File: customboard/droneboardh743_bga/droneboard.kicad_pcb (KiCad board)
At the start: 4 copper layers, 38 x 38 mm, 67 parts, among them J1 Conn_01x04_MountingPin, J10 Conn_01x03_Pin, J2 Conn_01x04_MountingPin, J3 Conn_01x08_MountingPin, J4 Conn_01x08_MountingPin, J5 USB_C_Receptacle_USB2.0_16P, J6 Conn_01x06_MountingPin, J7 Conn_01x06_MountingPin, Q1 DMN3042L, SW1 434133025816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

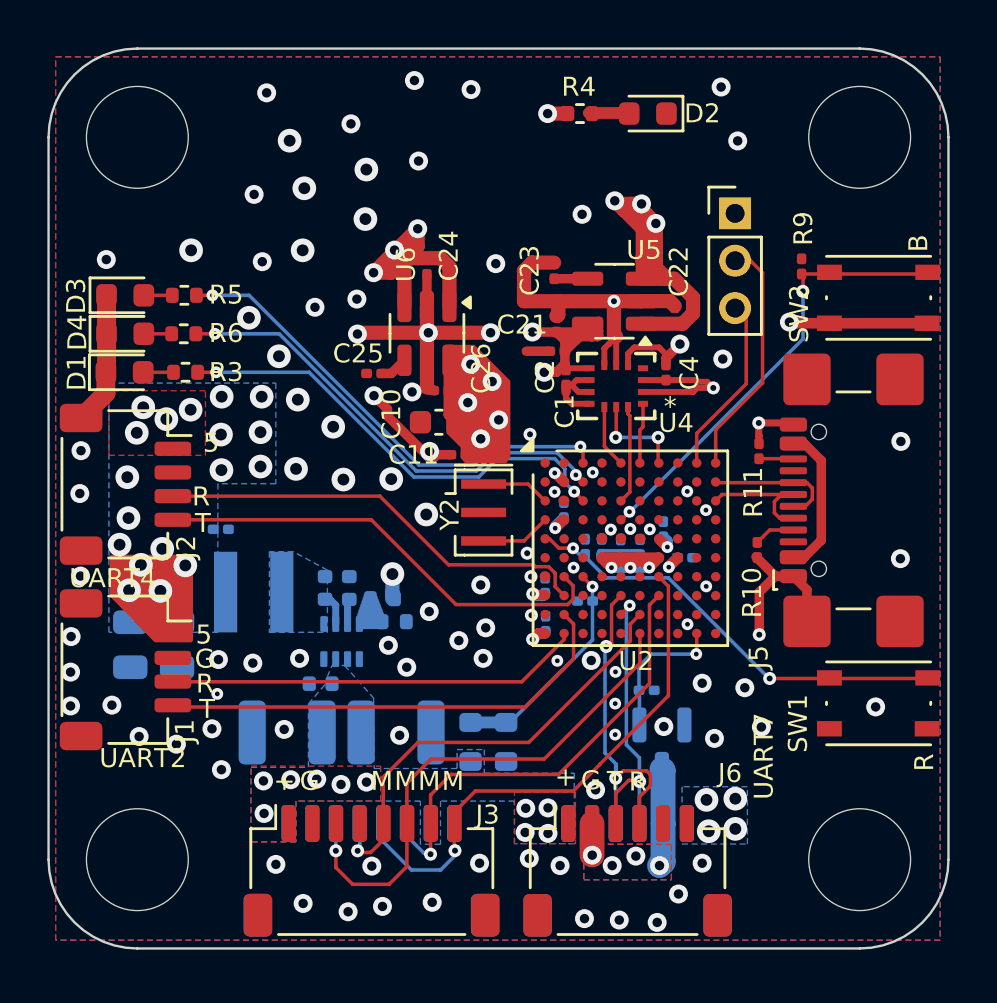
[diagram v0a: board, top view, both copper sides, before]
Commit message: pmos vtx power switching initial
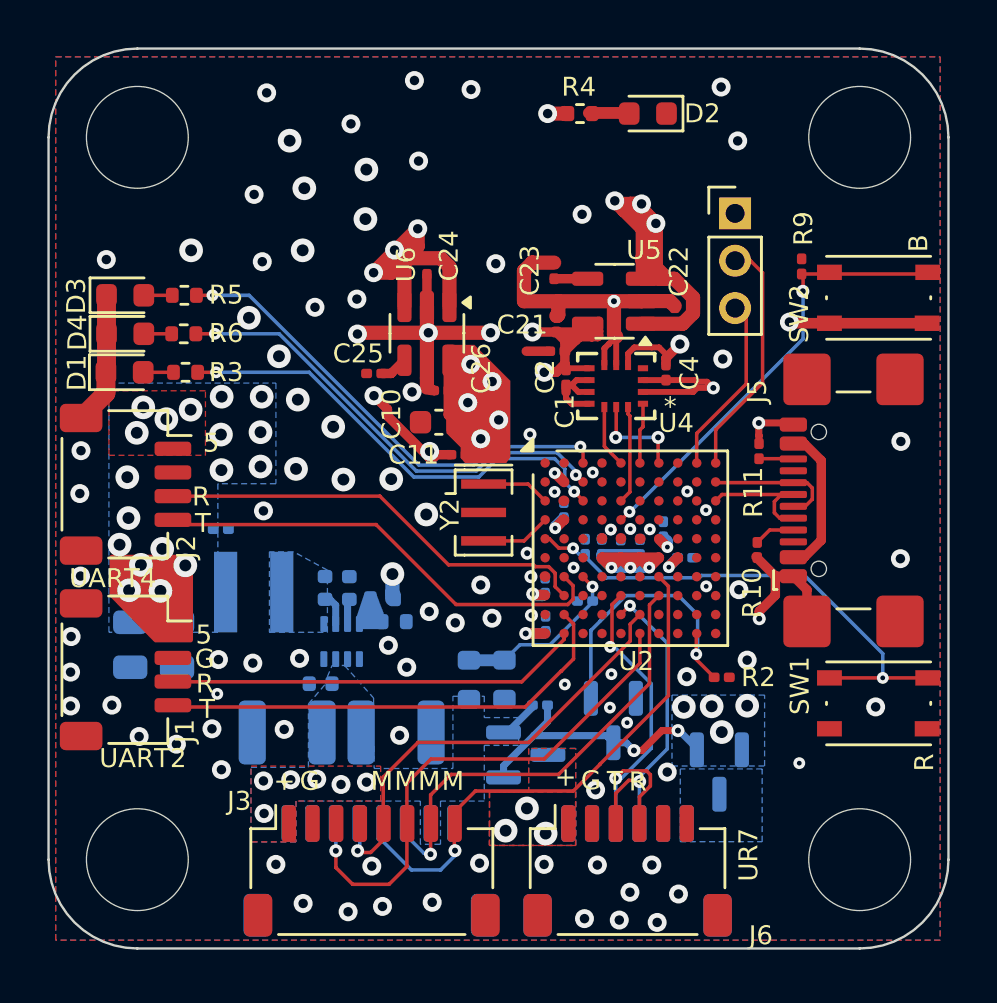
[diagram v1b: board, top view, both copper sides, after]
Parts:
- added Q2: DMP3056L, Package_TO_SOT_SMD:SOT-23, B.Cu at (70.2, 111.8)
- added Q3: DMP3056L, Package_TO_SOT_SMD:SOT-23, B.Cu at (78.3, 112.5)
- added R2: 10K, Resistor_SMD:R_0201_0603Metric, F.Cu at (78.4, 108.5)
- Q1: value DMN3042L -> BSS138-7-F
- moved R1 4.55 mm to (70.8, 109.7)
- moved R8 2.63 mm to (69.2, 108.7)
- moved R7 2.63 mm to (67.8, 108.7)
- moved Q1 2.34 mm to (73.8, 110.4)
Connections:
- J6 pad 1: /12V -> /VTX_12V
- J6 pad 2: /VTX_GND -> /GND
- J7 pad 1: /5V -> /VTX_5V
- J7 pad 2: /VTX_GND -> /GND
- Q1 pad 3: /VTX_GND -> /VTX_GATE
- R1 pad 1: /VTX_PWR -> /12V
- R1 pad 2: /GND -> /VTX_GATE
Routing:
- net /VTX_GATE: track 0.00 -> 11.7 mm, vias 0 -> 2
- net /VTX_PWR: track 5.99 -> 12.2 mm
- net /VTX_GND: track 5.48 -> 0.00 mm, vias 4 -> 0
- net /RESET1: track 18.6 -> 21.6 mm
- net /VBATMON: track 9.43 -> 7.48 mm
- net /12V: track 0.02 -> 1.77 mm, vias 10 -> 6
- net /U7TX: track 12.7 -> 13.6 mm
- net /GND: track 56.4 -> 55.8 mm, vias 105 -> 104
- net /U7RX: track 14.7 -> 15.3 mm
- net /VTX_12V: vias 0 -> 3
- added copper zone on B.Cu, net /VTX_12V
- added copper zone on F.Cu, net /VTX_12V
- added copper zone on B.Cu, net /VTX_5V
- removed copper zone on B.Cu, net /VTX_GND
- removed copper zone on F.Cu, net /VTX_GND
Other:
- board text added: "UR7"
- board text removed: "UART7"
